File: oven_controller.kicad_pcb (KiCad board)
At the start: 2 copper layers, 45 x 45 mm, 35 parts, among them CON1 BUQ2-USB-MICRO-B, IC1 BUQ2-ATXMEGA128A4U-A, P1 CONN_THERMO, P2 CONN_POWER, U1 FLASH_MEMORY, U2 MAX6675ISA+, U3 TAG-CONNECT-ATMEL-PDI-CONNECT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, U4 LD1117-SOT-223, U5 LS013B4DN04, U6 SW_PUSH_4_PIN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

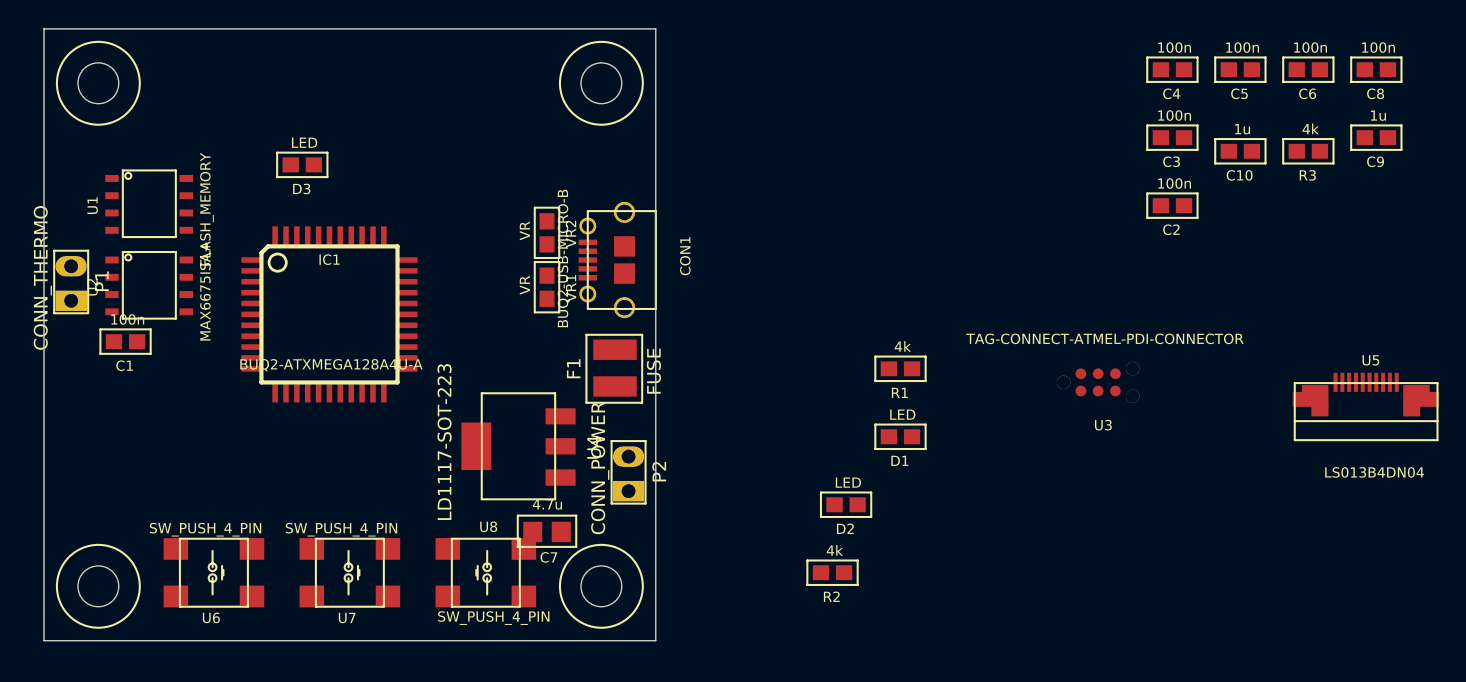
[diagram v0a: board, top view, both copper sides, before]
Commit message: Layout done, but not checked
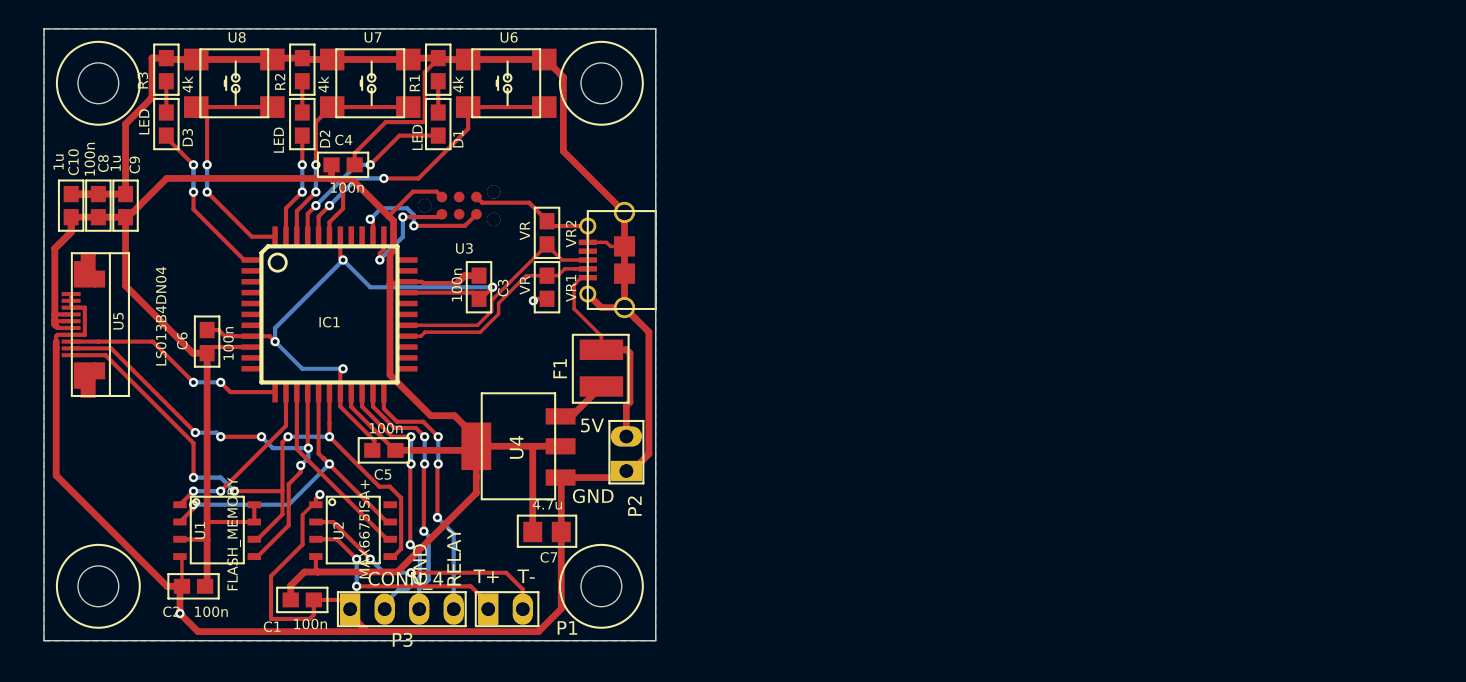
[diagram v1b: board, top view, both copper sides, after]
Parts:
- added P3: CONN_4, buq2:PIN_HEADER_4, F.Cu at (96.5, 106.7)
- moved C8 94.5 mm to (78.0, 77.0), turned to 90 degrees
- moved U5 93.0 mm to (76.0, 88.0), turned to 90 degrees
- moved C9 92.1 mm to (80.0, 77.0), turned to 90 degrees
- moved C10 86.1 mm to (76.0, 77.0), turned to 90 degrees
- moved R3 84.2 mm to (83.0, 67.0), turned to 270 degrees
- moved C6 83.4 mm to (86.0, 87.0), turned to 270 degrees
- moved C2 77.3 mm to (85.0, 105.0)
- moved C5 68.9 mm to (99.0, 95.0)
- moved C4 61.4 mm to (96.0, 74.0), turned to 180 degrees
- moved R2 53.8 mm to (93.0, 67.0), turned to 270 degrees
- moved C3 52.2 mm to (106.0, 83.0), turned to 90 degrees
- moved D2 48.8 mm to (93.0, 71.0), turned to 90 degrees
- moved U3 48.8 mm to (102.0, 77.0)
- moved U6 41.9 mm to (108.0, 68.0), turned to 0 degrees
- moved D1 41.0 mm to (103.0, 71.0), turned to 90 degrees
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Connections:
- IC1 pad 1: (no net) -> /LD2
- IC1 pad 12: (no net) -> /CS_DISPLAY
- IC1 pad 13: (no net) -> /CSn_FLASH
- IC1 pad 14: (no net) -> /nCS_THERMO
- IC1 pad 20: (no net) -> /RELAY0
- IC1 pad 21: (no net) -> /RELAY1
- IC1 pad 22: (no net) -> /RELAY2
- IC1 pad 28: /CSn_FLASH -> (no net)
- IC1 pad 29: /nCS_THERMO -> (no net)
- IC1 pad 32: /CS_DISPLAY -> (no net)
- IC1 pad 4: /BTN0 -> (no net)
- IC1 pad 40: /LD0 -> /BTN0
- IC1 pad 41: /LD1 -> /LD0
- IC1 pad 42: /LD2 -> /BTN1
- IC1 pad 43: (no net) -> /LD1
- IC1 pad 44: (no net) -> /BTN2
- IC1 pad 5: /BTN1 -> (no net)
- IC1 pad 6: /BTN2 -> (no net)
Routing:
- net GND: track 0.00 -> 254.4 mm, vias 0 -> 7
- net /VDD: track 0.00 -> 166.2 mm
- net /SCK: track 0.00 -> 48.2 mm, vias 0 -> 4
- net /MOSI: track 0.00 -> 34.4 mm, vias 0 -> 5
- net /MISO: track 0.00 -> 25.4 mm, vias 0 -> 2
- net /BTN0: track 0.00 -> 22.4 mm, vias 0 -> 2
- net /RELAY0: track 0.00 -> 20.0 mm, vias 0 -> 3
- net /RELAY1: track 0.00 -> 19.9 mm, vias 0 -> 3
- net /RELAY2: track 0.00 -> 19.7 mm, vias 0 -> 3
- net /T-: track 0.00 -> 18.7 mm, vias 0 -> 2
- net /BTN2: track 0.00 -> 18.5 mm, vias 0 -> 2
- net /D+: track 0.00 -> 16.7 mm
- net /CS_DISPLAY: track 0.00 -> 16.5 mm, vias 0 -> 2
- net /BTN1: track 0.00 -> 16.3 mm, vias 0 -> 2
- net /T+: track 0.00 -> 16.2 mm, vias 0 -> 2
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- added copper zone on B.Cu, net GND
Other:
- net class Default: clearance 0.254 -> 0.1524; trace_width 0.254 -> 0.1524; via_dia 0.889 -> 0.6858; via_drill 0.635 -> 0.3302
- rule trace_clearance: 0.254 -> 0.1524
- rule trace_min: 0.254 -> 0.1524
- rule via_min_drill: 0.508 -> 0.3302
- rule via_min_size: 0.889 -> 0.6858
- board text added: "5V"
- board text added: "CHECK DISPLAY CONNECTOR! More relays?"
- board text added: "GND"
- board text added: "RELAY"
- board text added: "T+"
- board text added: "T-"

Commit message: Ordered v1
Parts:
- added C11: 100n, buq2:SM0603, F.Cu at (90.5, 102.5)
- added P4: CONN_THERMO1, buq2:PIN_HEADER_2, F.Cu at (96.5, 106.2)
- added U9: MAX6675ISA+, buq2:8-SOIC, F.Cu at (89.5, 97.0)
- P1: value CONN_THERMO -> CONN_THERMO0
- moved U3 10.8 mm to (112.0, 73.0)
- moved P3 10.2 mm to (86.4, 106.2)
- moved C1 6.26 mm to (98.5, 103.0)
- moved P1 5.10 mm to (101.6, 106.2)
- moved U2 3.81 mm to (97.5, 97.5)
- moved U1 3.20 mm to (81.5, 97.0)
- moved C2 2.69 mm to (84.0, 102.5), turned to 180 degrees
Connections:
- net /T+ renamed /T+0
- net /T- renamed /T-0
- IC1 pad 10: (no net) -> /CS_DISPLAY
- IC1 pad 11: (no net) -> /CSn_FLASH
- IC1 pad 12: /CS_DISPLAY -> /nCS_THERMO1
- IC1 pad 13: /CSn_FLASH -> /nCS_THERMO0
- IC1 pad 14: /nCS_THERMO -> (no net)
- U2 pad 6: /nCS_THERMO -> /nCS_THERMO0
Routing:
- net GND: track 254.4 -> 198.2 mm, vias 7 -> 15
- net /VDD: track 166.2 -> 196.1 mm
- net /nCS_THERMO0: track 0.00 -> 18.7 mm
- net /T-1: track 0.00 -> 17.4 mm
- net /MISO: track 25.4 -> 42.5 mm, vias 2 -> 0
- net /nCS_THERMO: track 13.8 -> 0.00 mm
- net /PDI_DATA: track 8.66 -> 20.7 mm
- net /PDI_CLK: track 10.9 -> 22.6 mm
- net /nCS_THERMO1: track 0.00 -> 10.6 mm, vias 0 -> 2
- net /T+1: track 0.00 -> 10.0 mm
- net /T-0: track 18.7 -> 10.6 mm, vias 2 -> 0
- net /T+0: track 16.2 -> 8.56 mm, vias 2 -> 0
- net /MOSI: track 34.4 -> 31.1 mm, vias 5 -> 4
- net /SCK: track 48.2 -> 51.3 mm
- net /CS_DISPLAY: track 16.5 -> 14.2 mm, vias 2 -> 0
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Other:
- board text added: "Oven controller V1 2015-01-21 Matti Jukola"
- board text added: "REL0"
- board text added: "REL1"
- board text added: "REL2"
- board text added: "T+0"
- board text added: "T+1"
- board text added: "T-0"
- board text added: "T-1"
- board text removed: "CHECK DISPLAY CONNECTOR! More relays?"
- board text removed: "RELAY"
- board text removed: "T+"
- board text removed: "T-"
